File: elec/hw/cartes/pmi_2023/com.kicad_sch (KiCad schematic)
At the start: 31 parts, among them J7 USB4105-GF-A-060, Q2 2N7002, SW7 MSS12C02LS-BB2.0, U32 ESP32-S3-WROOM-1

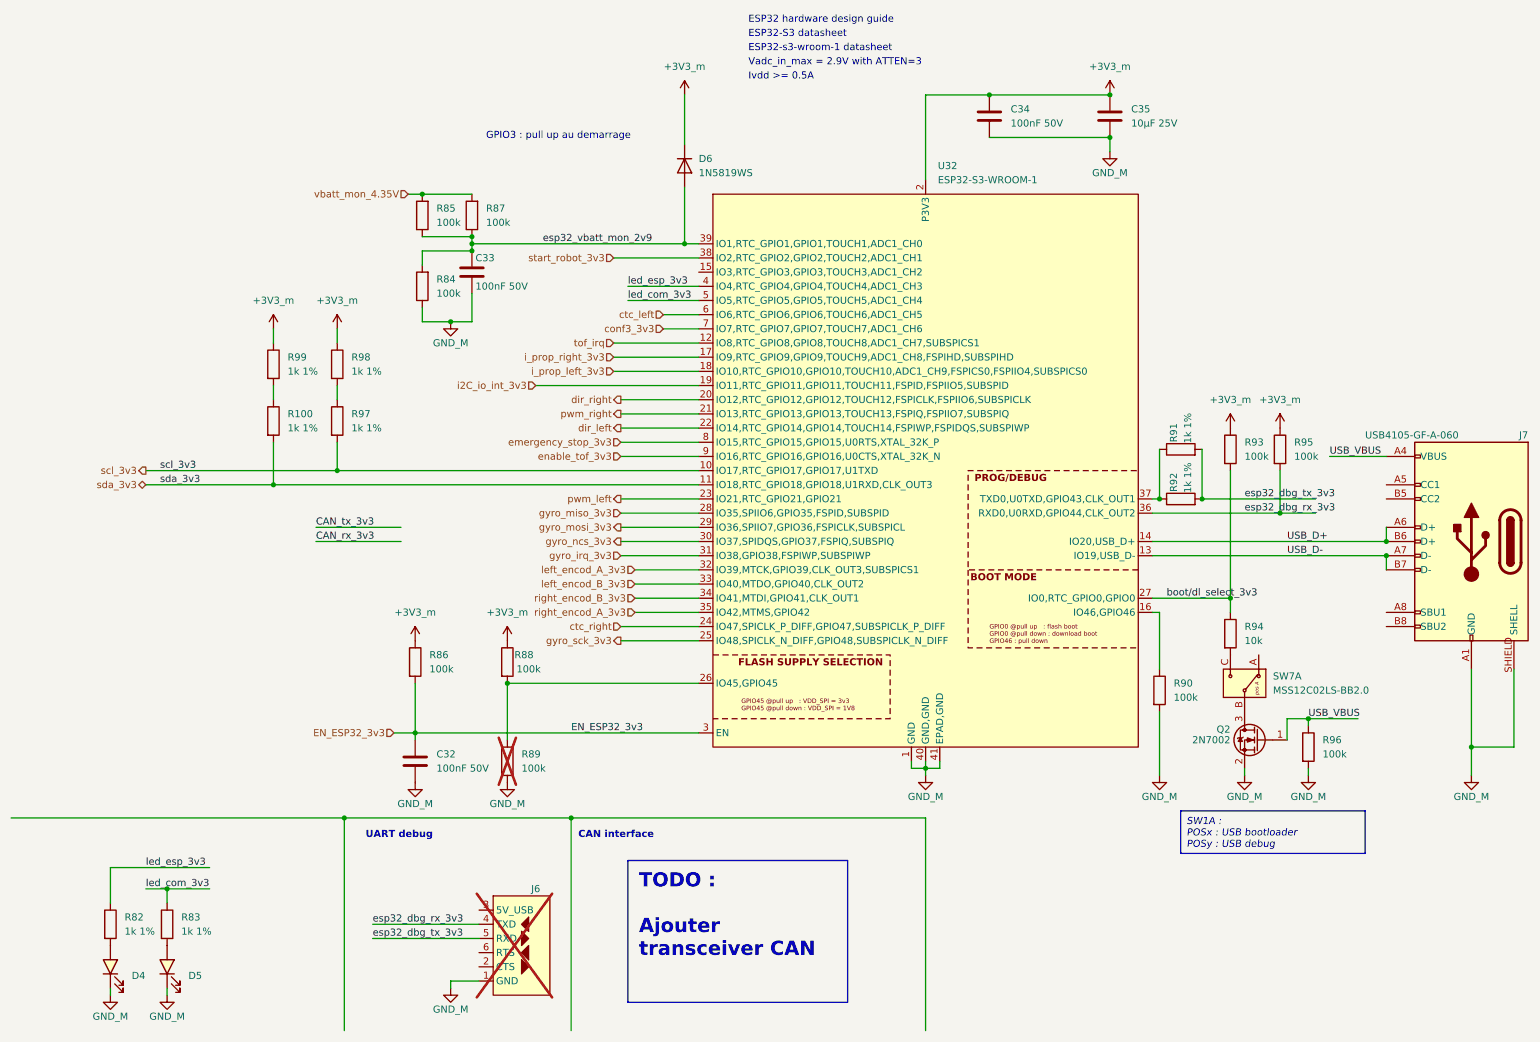
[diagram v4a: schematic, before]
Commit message: added oled display power supply res selectors, jlcpcb refs : wip
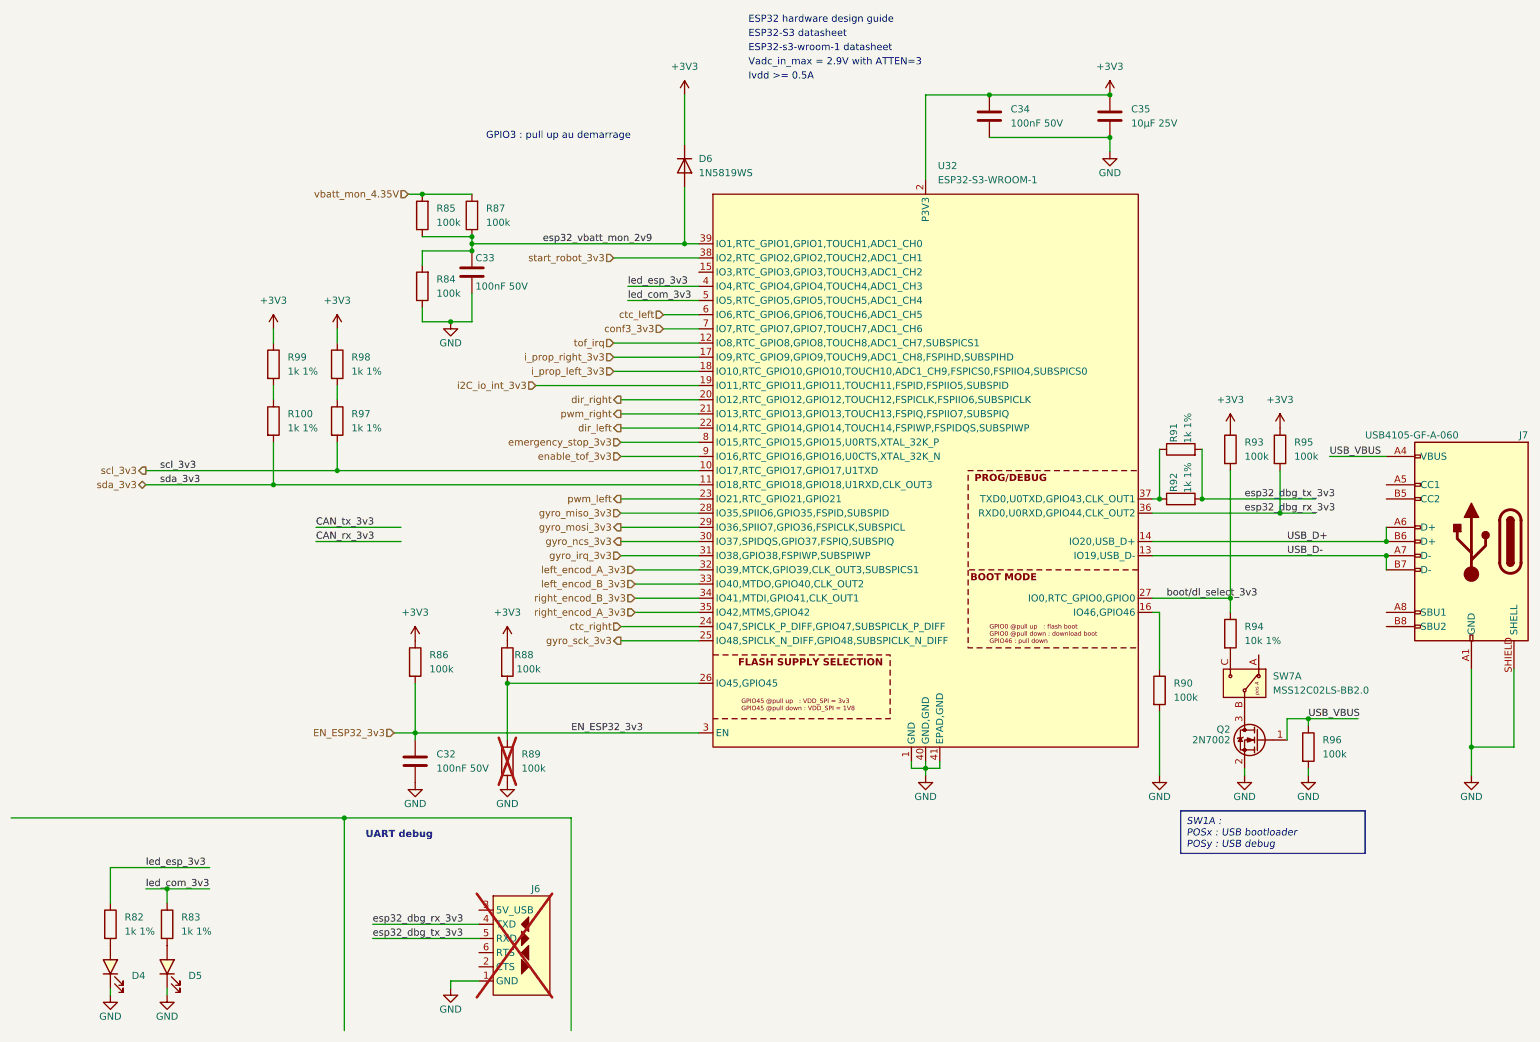
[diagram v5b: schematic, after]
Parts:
- C35: symbol cocotter_capacitors:C_10µF_16V_0805_X5R -> cocotter_capacitors:C_10µF_25V_0805_X5R; Specification 10µF 25V X5R 0805 -> 10µF 25V X7R 0805
- D4, D5: value red, 0603 -> white, 0603
- R94: value 10k -> 10k 1%
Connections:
- net at R82.2: now also D4.2 (A); no longer D4.A
- net at R83.2: now also D5.2 (A); no longer D5.A
- net +3V3_m renamed +3V3
- net GND_M renamed GND
- net GND: now also D4.1 (K), D5.1 (K); no longer D4.C, D5.C
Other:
- note removed: "CAN interface"
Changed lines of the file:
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@@
 	)
 	(junction
-		(at 111.76 158.75)
-		(diameter 0)
-		(color 0 0 0 0)
-	)
-	(junction
 		(at 39.37 171.45)
 		(diameter 0)
@@
 	(wire
 		(pts
-			(xy 175.26 196.85) (xy 175.26 158.75)
-		)
-		(stroke
-			(width 0)
-			(type dash)
-		)
-	)
-	(wire
-		(pts
 			(xy 100.33 144.78) (xy 100.33 134.62)
 		)
@@
 	(wire
 		(pts
-			(xy 111.76 158.75) (xy 175.26 158.75)
-		)
-		(stroke
-			(width 0)
-			(type dash)
-		)
-	)
-	(wire
-		(pts
 			(xy 85.09 69.85) (xy 90.17 69.85)
 		)
@@
 		)
 	)
-	(text_box "TODO : \n\nAjouter transceiver CAN"
-		(exclude_from_sim no)
-		(at 121.92 166.37 0)
-		(size 39.37 25.4)
-		(stroke
-			(width 0)
-			(type default)
-		)
-		(fill
-			(type color)
-			(color 255 0 0 1)
-		)
-		(effects
-			(font
-				(size 2.54 2.54)
-				(thickness 0.508)
-				(bold yes)
-			)
-			(justify left top)
-		)
-	)
 	(text "GPIO3 : pull up au demarrage"
 		(exclude_from_sim no)
@@
 		)
 	)
-	(text "CAN interface"
-		(exclude_from_sim no)
-		(at 113.03 162.56 0)
-		(effects
-			(font
-				(size 1.27 1.27)
-				(thickness 0.254)
-				(bold yes)
-			)
-			(justify left bottom)
-		)
-	)
 	(text "ESP32 hardware design guide"
 		(exclude_from_sim no)
@@
 	)
 	(symbol
-		(lib_id "cocotter_capacitors:C_10µF_16V_0805_X5R")
+		(lib_id "cocotter_capacitors:C_10µF_25V_0805_X5R")
 		(at 208.28 33.02 0)
 		(unit 1)
@@
 			)
 		)
-		(property "Description" ""
+		(property "Description" "Unpolarized capacitor"
 			(at 208.28 33.02 0)
 			(effects
@@
 			)
 		)
-		(property "Specification" "10µF 25V X5R 0805 "
+		(property "Specification" "10µF 25V X7R 0805 "
 			(at 208.28 33.02 0)
 			(effects
@@
 			)
 		)
-		(property "Value" "+3V3_m"
+		(property "Value" "+3V3"
 			(at 100.33 121.92 0)
 			(effects
@@
 			)
 		)
-		(property "Value" "GND_M"
+		(property "Value" "GND"
 			(at 90.17 73.66 0)
 			(effects
@@
 			)
 		)
-		(property "Value" "GND_M"
+		(property "Value" "GND"
 			(at 100.33 156.21 0)
 			(effects
@@
 			)
 		)
-		(property "Description" "Unpolarized capacitor"
+		(property "Description" "Unpolarized capacitor tol +/-10%"
 			(at 186.69 33.02 0)
 			(effects
@@
 			)
 		)
-		(property "Value" "GND_M"
+		(property "Value" "GND"
 			(at 90.17 193.04 0)
 			(effects
@@
 			)
 		)
-		(property "Value" "GND_M"
+		(property "Value" "GND"
 			(at 232.41 154.94 0)
 			(effects
@@
 			)
 		)
-		(property "Value" "GND_M"
+		(property "Value" "GND"
 			(at 175.26 154.94 0)
 			(effects
@@
 			)
 		)
-		(property "Value" "GND_M"
+		(property "Value" "GND"
 			(at 243.84 154.94 0)
 			(effects
@@
 			)
 		)
-		(property "Value" "+3V3_m"
+		(property "Value" "+3V3"
 			(at 208.28 24.13 0)
 			(effects
@@
 			)
 		)
-		(property "Value" "GND_M"
+		(property "Value" "GND"
 			(at 217.17 154.94 0)
 			(effects
@@
 			)
 		)
-		(property "Value" "red, 0603"
+		(property "Value" "white, 0603"
 			(at 31.75 185.42 0)
 			(effects
@@
 			)
 		)
-		(property "Description" ""
+		(property "Description" "Light emitting diode, white, Vf=[2.6V; 3.1V]"
 			(at 29.21 185.42 0)
 			(effects
@@
 			)
 		)
-		(pin "C"
+		(pin "2"
 		)
-		(pin "A"
+		(pin "1"
 		)
 		(instances
@@
 			)
 		)
-		(property "Value" "10k"
+		(property "Value" "10k 1%"
 			(at 232.41 127 0)
 			(effects
@@
 			)
 		)
-		(property "Description" "Unpolarized capacitor"
+		(property "Description" "Unpolarized capacitor tol +/-10%"
 			(at 93.98 60.96 0)
 			(effects
@@
 			)
 		)
-		(property "Description" "Unpolarized capacitor"
+		(property "Description" "Unpolarized capacitor tol +/-10%"
 			(at 83.82 148.59 0)
 			(effects
@@
 			)
 		)
-		(property "Value" "GND_M"
+		(property "Value" "GND"
 			(at 39.37 194.31 0)
 			(effects
@@
 			)
 		)
-		(property "Value" "red, 0603"
+		(property "Value" "white, 0603"
 			(at 41.91 185.42 0)
 			(effects
@@
 			)
 		)
-		(property "Description" ""
+		(property "Description" "Light emitting diode, white, Vf=[2.6V; 3.1V]"
 			(at 39.37 185.42 0)
 			(effects
@@
 			)
 		)
-		(pin "A"
+		(pin "1"
 		)
-		(pin "C"
+		(pin "2"
 		)
 		(instances
@@
 			)
 		)
-		(property "Value" "GND_M"
+		(property "Value" "GND"
 			(at 273.05 154.94 0)
 			(effects
@@
 			)
 		)
-		(property "Value" "+3V3_m"
+		(property "Value" "+3V3"
 			(at 229.87 83.82 0)
 			(effects
@@
 			)
 		)
-		(property "Value" "+3V3_m"
+		(property "Value" "+3V3"
 			(at 238.76 83.82 0)
 			(effects
@@
 			)
 		)
-		(property "Value" "+3V3_m"
+		(property "Value" "+3V3"
 			(at 83.82 121.92 0)
 			(effects
@@
 			)
 		)
-		(property "Value" "+3V3_m"
+		(property "Value" "+3V3"
 			(at 132.08 24.13 0)
 			(effects
@@
 			)
 		)
-		(property "Value" "GND_M"
+		(property "Value" "GND"
 			(at 208.28 43.18 0)
 			(effects
@@
 			)
 		)
-		(property "Value" "+3V3_m"
+		(property "Value" "+3V3"
 			(at 58.42 66.04 0)
 			(effects
@@
 			)
 		)
-		(property "Value" "GND_M"
+		(property "Value" "GND"
 			(at 83.82 156.21 0)
 			(effects
@@
 			)
 		)
-		(property "Value" "GND_M"
+		(property "Value" "GND"
 			(at 29.21 194.31 0)
 			(effects
@@
 			)
 		)
-		(property "Value" "+3V3_m"
+		(property "Value" "+3V3"
 			(at 69.85 66.04 0)
 			(effects

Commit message: reset button added to esp32 reset. uart prog connector replaces ftdi one
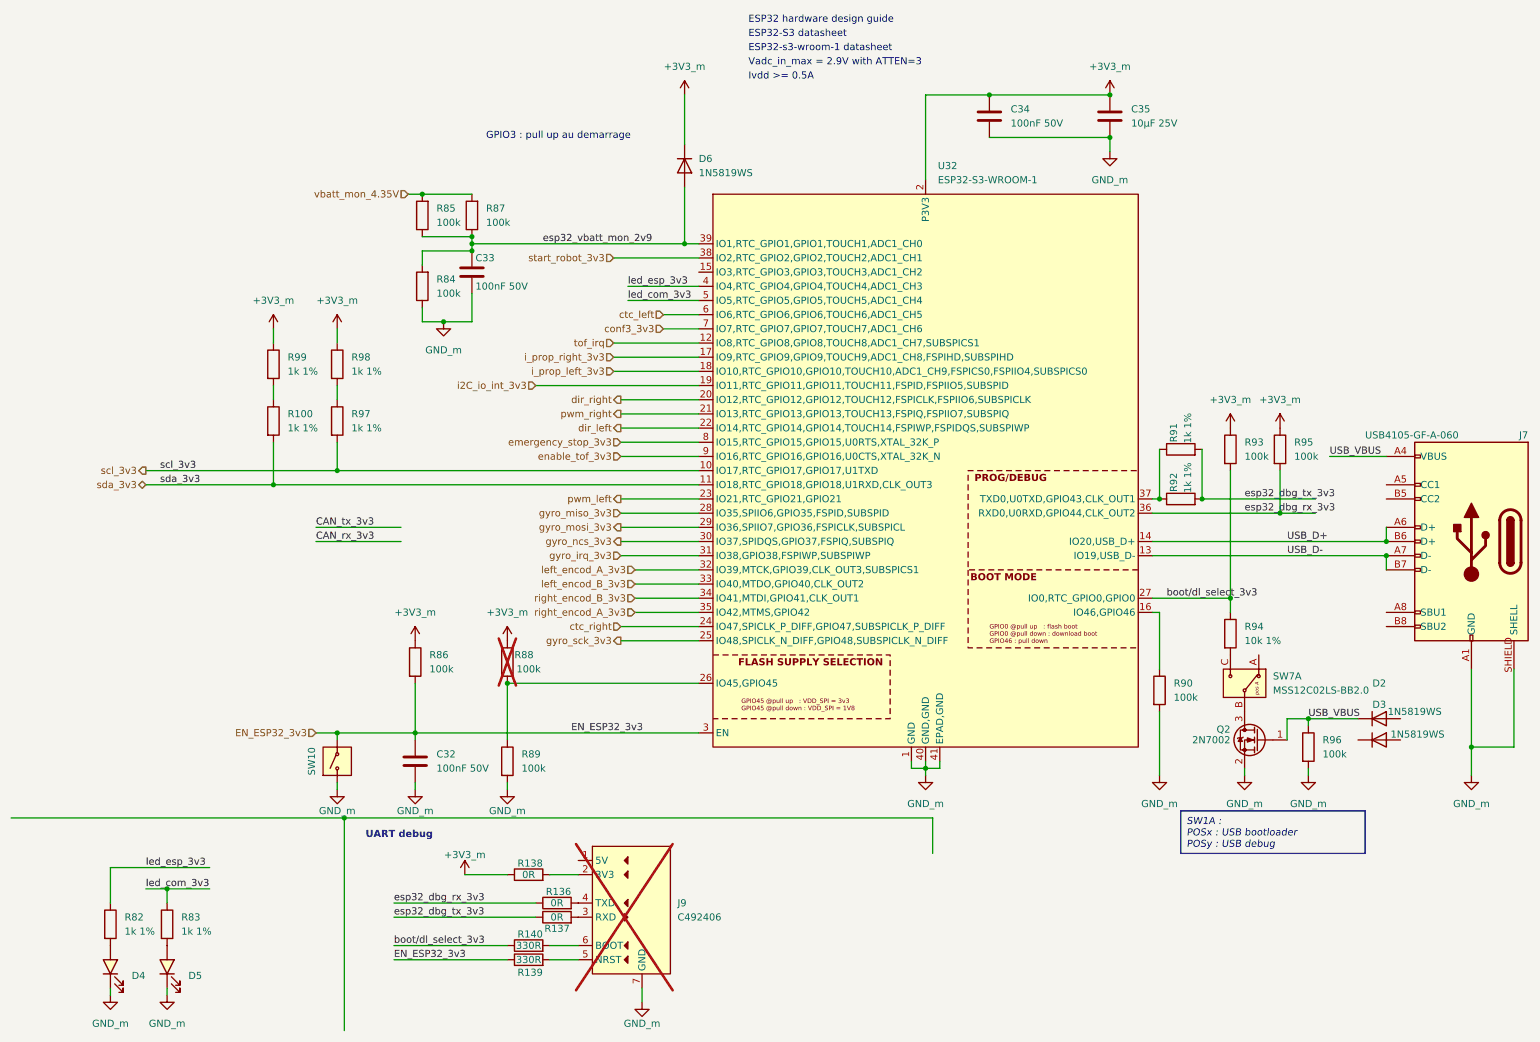
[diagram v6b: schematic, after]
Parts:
- removed J6: ~, cocotter_connectors:TTL-232R-3V3, symbol cocotter_connectors:TTL-232R-3V3
- added D2, D3: 1N5819WS, cocotter_diodes:D_SOD-323F, symbol cocotter_diodes:1N5819WS
- added J9: ~, cocotter_connectors:eps32_uart_programmer, symbol cocotter_connectors:eps32_uart_programmer
- added R136, R137, R138: 0R, cocotter_resistor:r0603_reflow, symbol cocotter_resistors:R_0R_0603
- added R139, R140: 330R, cocotter_resistor:r0603_reflow, symbol cocotter_resistors:R_330R_0603_1%
- added SW10: TS-1187A-B-A-B, cocotter_others:TS-1187A-B-A-B, symbol cocotter_others:TS-1187A-B-A-B
- D4, D5: footprint cocotter_diodes:LED_0603_1608Metric -> (none)
- R88: now not fitted
- R89: now fitted
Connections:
- net EN_ESP32_3v3: now also R139.1, SW10.B (2)
- net USB_VBUS: now also D2.1 (K)
- net boot/dl_select_3v3: now also R140.1
- net esp32_dbg_rx_3v3: now also R136.1
- net esp32_dbg_tx_3v3: now also R137.1
- net +3V3 renamed +3V3_m
- net +3V3_m: now also R138.1
- net GND renamed GND_m
- net GND_m: now also J9.7 (GND), SW10.A (1)
- new net: J9.6 (BOOT), R140.2
- new net: J9.5 (NRST), R139.2
- new net: J9.3 (RXD), R137.2
- new net: J9.2 (3V3), R138.2
- new net: J9.4 (TXD), R136.2

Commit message: pmi2023 : drc cleanup
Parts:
- removed D2, D3: 1N5819WS, cocotter_diodes:D_SOD-323F, symbol cocotter_diodes:1N5819WS
- D4, D5: footprint (none) -> cocotter_diodes:LED_0603_1608Metric
- J7: symbol cocotter_connectors:USB4105-GF-A-060 -> cocotter_connectors:USB-TYPE-C-019; JLCPCB C2927300 -> C2927039
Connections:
- net GND_m: now also D4.C, D5.C; no longer D4.1 (C), D5.1 (C)
- net at R82.2: now also D4.A; no longer D4.2 (A)
- net at R83.2: now also D5.A; no longer D5.2 (A)
- net enable_back_tof_3v3: now reaches U32.15 (IO3,RTC_GPIO3,GPIO3,TOUCH3,ADC1_CH2)
- net enable_tof_3v3 renamed enable_front_tof_3v3
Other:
- moved on the sheet: C32, R86, R88, R89

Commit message: routing cleanup, test points added to allow charging of battery in the pmi
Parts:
- R85: now not fitted
- R87: symbol cocotter_resistors:R_100k_0603_1% -> cocotter_resistors:R_91k_0603_1%; JLCPCB C25803 -> C23265; Specification 100k 0603 1% 100mW -> 91k 0603 1% 100mW
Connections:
- net esp32_vbatt_mon_2v9 renamed esp32_vbatt_mon_1v8
- net vbatt_mon_4.35V renamed vbatt_mon_3.45V
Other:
- note removed: "GPIO3 : pull up au demarrage"
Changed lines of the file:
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@@
 		)
 	)
-	(text_box "SW1A : \n  POS A : USB bootloader\n  POS B : USB debug"
+	(text_box "Vbat_mon voltage :\n- Li-ion : 4.35V max\n- LiFePO4 : 3.45V max\n=>with Li-ion esp32_vbatt_mon max = 2.3V"
 		(exclude_from_sim no)
-		(at 220.98 157.48 0)
-		(size 33.02 7.62)
+		(at 85.09 31.75 0)
+		(size 33.02 11.43)
 		(stroke
 			(width 0)
@@
 		)
 	)
-	(text "GPIO3 : pull up au demarrage"
+	(text_box "SW1A : \n  POS A : USB bootloader\n  POS B : USB debug"
 		(exclude_from_sim no)
-		(at 109.474 36.576 0)
+		(at 220.98 157.48 0)
+		(size 33.02 7.62)
+		(stroke
+			(width 0)
+			(type default)
+		)
+		(fill
+			(type color)
+			(color 0 194 0 1)
+		)
 		(effects
 			(font
 				(size 1.27 1.27)
+				(italic yes)
+				(color 255 255 255 1)
 			)
+			(justify left top)
 		)
 	)
@@
 		)
 	)
-	(label "esp32_vbatt_mon_2v9"
+	(label "esp32_vbatt_mon_1v8"
 		(at 106.68 55.88 0)
 		(fields_autoplaced yes)
@@
 		)
 	)
-	(hierarchical_label "vbatt_mon_4.35V"
+	(hierarchical_label "vbatt_mon_3.45V"
 		(shape input)
 		(at 82.55 46.99 180)
@@
 	)
 	(symbol
-		(lib_id "cocotter_resistors:R_100k_0603_1%")
+		(lib_id "cocotter_resistors:R_91k_0603_1%")
 		(at 93.98 50.8 180)
 		(unit 1)
@@
 			)
 		)
-		(property "Specification" "100k 0603 1% 100mW"
+		(property "Specification" "91k 0603 1% 100mW"
 			(at 93.98 50.8 0)
 			(effects
@@
 			)
 		)
-		(property "JLCPCB" "C25803"
+		(property "JLCPCB" "C23265"
 			(at 93.98 50.8 0)
 			(effects
@@
 		(in_bom yes)
 		(on_board yes)
-		(dnp no)
+		(dnp yes)
 		(fields_autoplaced yes)
 		(property "Reference" "R85"
